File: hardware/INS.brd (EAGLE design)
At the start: 47 x 40.5 mm, 47 parts, among them IC1 BN055, IC3 BME280, J1 MICRO_USB_B_HIROSE_ZX62-B-5PA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, U1 NEO-M9N-00B, U2 STM32L433CCT6

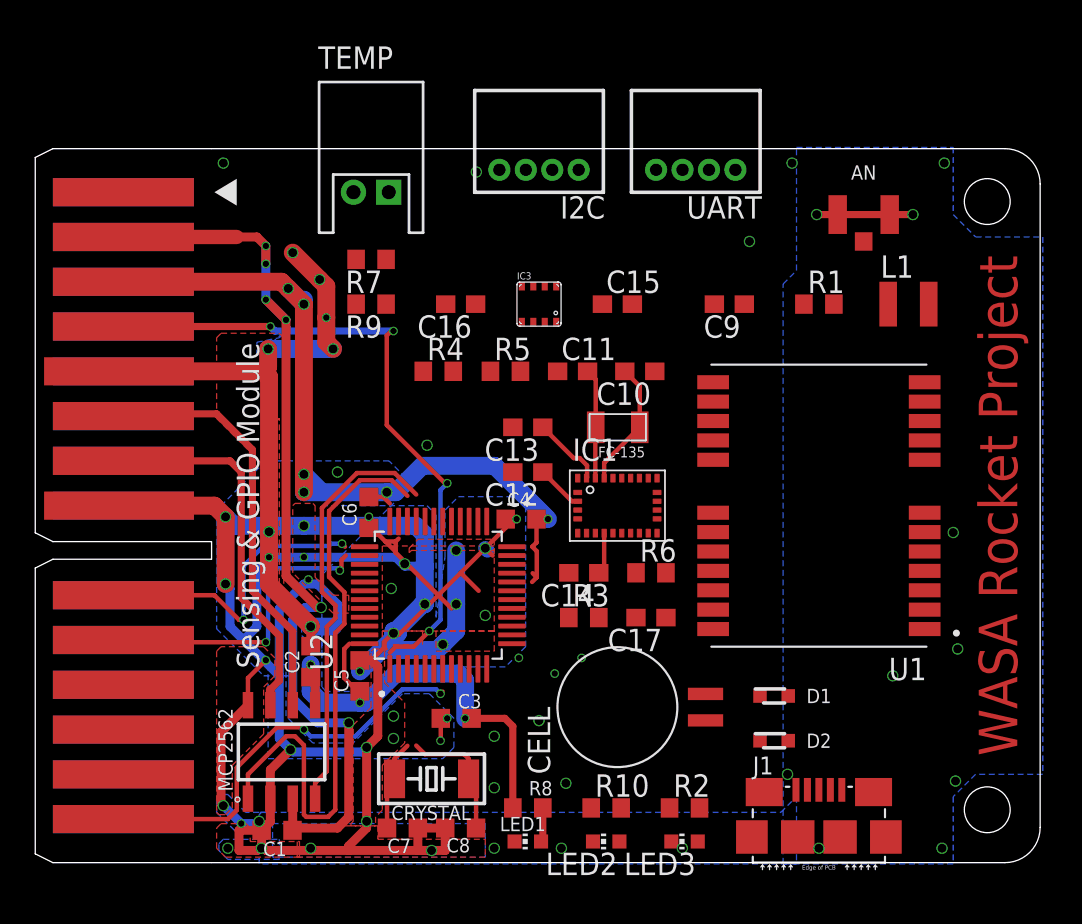
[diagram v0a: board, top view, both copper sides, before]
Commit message: BatteryPowerV2とINSの基板設計です。変えたつもりはないんですけど、schの方が変わっちゃってる可能性があって、申し訳ないんですけど確認お願いします。
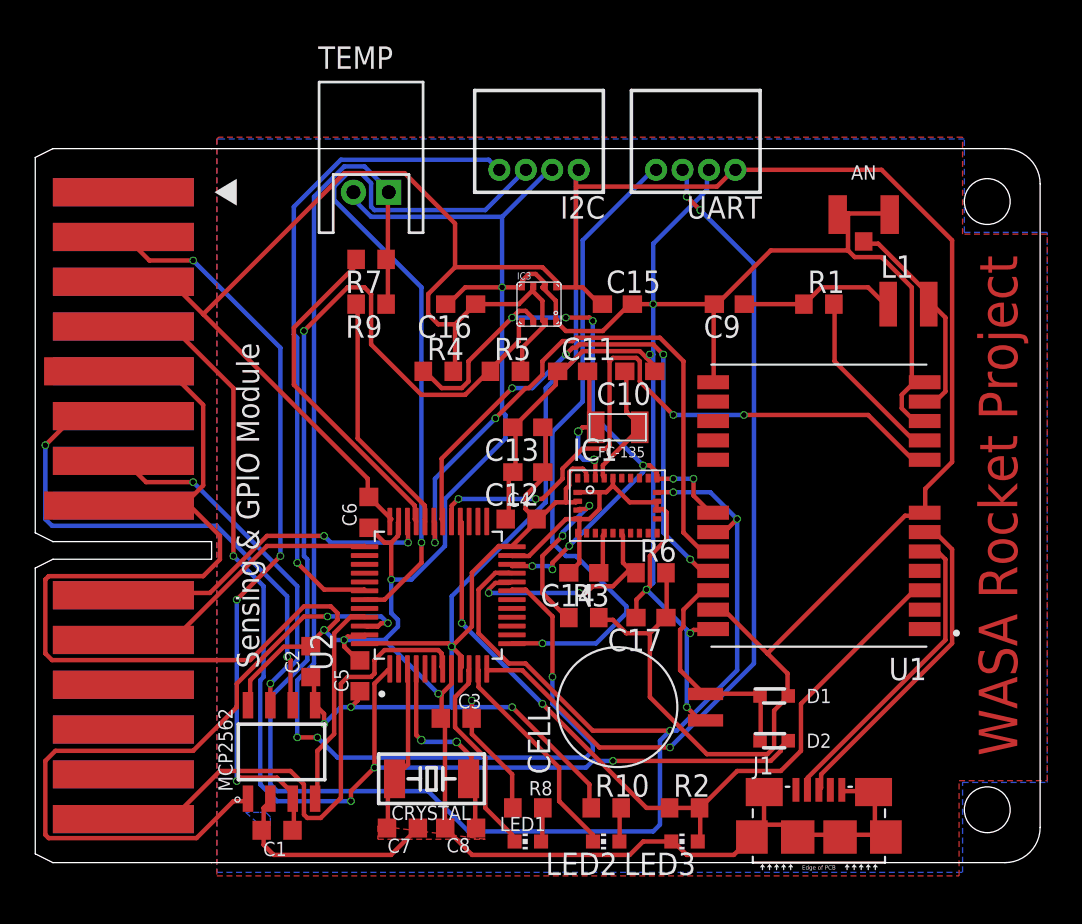
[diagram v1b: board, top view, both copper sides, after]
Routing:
- net VDD: track 81.9 -> 251.6 mm, vias 9 -> 5
- net I2C2_SCL: track 0.00 -> 114.2 mm, vias 0 -> 4
- net GND: track 202.3 -> 307.9 mm, vias 66 -> 10
- net TEMP: track 0.00 -> 72.2 mm, vias 0 -> 3
- net UART_TRX: track 0.00 -> 48.7 mm, vias 0 -> 3
- net 1PPS: track 0.00 -> 45.1 mm, vias 0 -> 2
- net I2C1_SDA: track 0.00 -> 41.3 mm, vias 0 -> 1
- net I2C2_SDA: track 0.00 -> 39.9 mm, vias 0 -> 9
- net I2C1_SCL: track 0.00 -> 37.8 mm, vias 0 -> 1
- net GPS_!RESET!: track 0.00 -> 37.4 mm, vias 0 -> 4
- net UART_RTX: track 0.00 -> 37.0 mm, vias 0 -> 1
- net GPS_RTX: track 0.00 -> 35.1 mm, vias 0 -> 2
- net GPS_TRX: track 0.00 -> 32.9 mm, vias 0 -> 4
- net VBAT: track 37.3 -> 69.1 mm
- net TEMP_HIGH: track 0.00 -> 19.2 mm
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
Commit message: 大変お待たせしました。BatteryPowerV2とINSの改良版です。確認お願いします。
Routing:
- net VDD: track 251.6 -> 298.7 mm, vias 5 -> 15
- net GND: track 307.9 -> 288.9 mm, vias 10 -> 26
- net I2C1_SDA: track 41.3 -> 30.5 mm
- net VCC: track 42.9 -> 50.7 mm
- net USB_D+: track 18.7 -> 22.9 mm
- net N$11: track 13.4 -> 16.8 mm
- net N$4: track 30.4 -> 27.5 mm, vias 0 -> 2
- net TEMP: track 72.2 -> 69.3 mm
- net UART_TRX: track 48.7 -> 50.9 mm, vias 3 -> 1
- net VBAT: track 69.1 -> 71.1 mm
- net I2C2_SCL: track 114.2 -> 115.9 mm
- net GPS_RTX: track 35.1 -> 36.7 mm
- net USB_D-: track 17.7 -> 19.3 mm
- net I2C1_SCL: track 37.8 -> 39.1 mm
- net CAN_TX: track 41.9 -> 43.1 mm
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
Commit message: 微調整
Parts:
- moved R10 1.02 mm to (32.4, -16.1)
- moved R2 1.02 mm to (36.8, -16.1)
- moved R8 1.02 mm to (27.9, -16.1)
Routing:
- net GND: track 288.9 -> 254.5 mm, vias 26 -> 198
- net CAN_TX: track 43.1 -> 19.4 mm
- net I2C2_SCL: track 115.9 -> 104.1 mm
- net CANL1: track 31.2 -> 24.1 mm
- net VDD: track 298.7 -> 292.8 mm
- net VBAT: track 71.1 -> 75.7 mm
- net TEMP_HIGH: track 19.6 -> 17.5 mm
- net USB_D-: track 19.3 -> 21.0 mm
- net 1PPS: track 45.5 -> 47.0 mm
- net CANH1: track 20.0 -> 21.2 mm
- net N$74: track 2.00 -> 3.02 mm
- net N$12: track 2.01 -> 3.02 mm
- net N$4: track 27.5 -> 26.5 mm, vias 2 -> 4
- net N$7: track 8.95 -> 9.80 mm
- net I2C1_SCL: track 39.1 -> 38.3 mm
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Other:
- board text added: "ERR"
- board text added: "GNSS"
- board text added: "INS Module"
- board text added: "STAT"
- board text added: "WASA Rocket 2023"
- board text removed: "Sensing & GPIO Module"
- board text removed: "WASA Rocket Project"
